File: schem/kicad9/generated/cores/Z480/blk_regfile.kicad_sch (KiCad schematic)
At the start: 0 parts

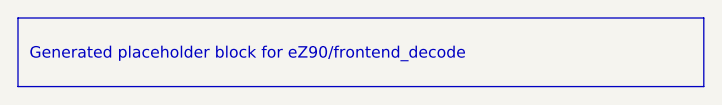
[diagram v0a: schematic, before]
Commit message: systems: rename CarbonEZ90 to CarbonZ480 and refresh maps
Detailed description:
- What changed: renamed the CarbonEZ90 system to CarbonZ480, updated system tops for Z480 tier IDs and boot signatures, refreshed memory map docs and carbon_memmap_pkg, and updated KiCad kicadgen specs plus regenerated Z480/CarbonZ480 schematics.
- Why it changed: keep system naming, maps, and schematics consistent with the new Z480 tier model.
- Files/paths affected: hdl/systems/CarbonZ480/*, hdl/systems/CarbonEZ90/* (removed), hdl/systems/CarbonZ80/*, hdl/systems/CarbonZ90/*, hdl/systems/CarbonX86/*, hdl/systems/CarbonX96/*, hdl/systems/common/rtl/carbon_memmap_pkg.sv, schem/kicad9/spec/kicadgen_*.yaml, schem/kicad9/generated/cores/Z480, schem/kicad9/generated/systems/CarbonZ480.
- Any compatibility notes: reset still enters P0; Z480 presents as P7; memory map ranges stay stable aside from naming.
- What remains TODO: update sim harnesses and documentation references to the new names.
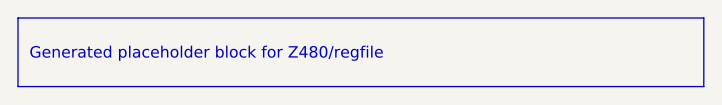
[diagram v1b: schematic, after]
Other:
- title: eZ90::frontend_decode -> Z480::regfile
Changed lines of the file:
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@@
 	(paper "A3")
 	(title_block
-		(title "eZ90::frontend_decode")
+		(title "Z480::regfile")
 		(company "Project Carbon")
 		(comment 1 "Generated - do not edit in generated/")
@@
 	)
 	(text_box
-		"Generated placeholder block for eZ90/frontend_decode"
+		"Generated placeholder block for Z480/regfile"
 		(exclude_from_sim no)
 		(at
